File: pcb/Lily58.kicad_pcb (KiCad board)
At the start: 2 copper layers, 142.5 x 106.3 mm, 112 parts, among them P4 OLED, SW1 SW_PUSH, SW10 SW_PUSH, SW11 SW_PUSH, SW12 SW_PUSH, SW13 SW_PUSH, SW14 SW_PUSH, SW15 SW_PUSH, SW16 SW_PUSH, SW17 SW_PUSH, SW18 SW_PUSH, SW19 SW_PUSH, SW2 SW_PUSH, SW20 SW_PUSH, SW21 SW_PUSH, SW22 SW_PUSH, SW23 SW_PUSH, SW24 SW_PUSH, SW25 Rotary_Encoder_Switch, SW26 SW_PUSH, SW27 SW_PUSH, SW28 SW_PUSH, SW29 SW_PUSH, SW3 SW_PUSH, SW4 SW_PUSH, SW5 SW_PUSH, SW6 SW_PUSH, SW7 SW_PUSH, SW8 SW_PUSH, SW9 SW_PUSH, U1 NiceNano

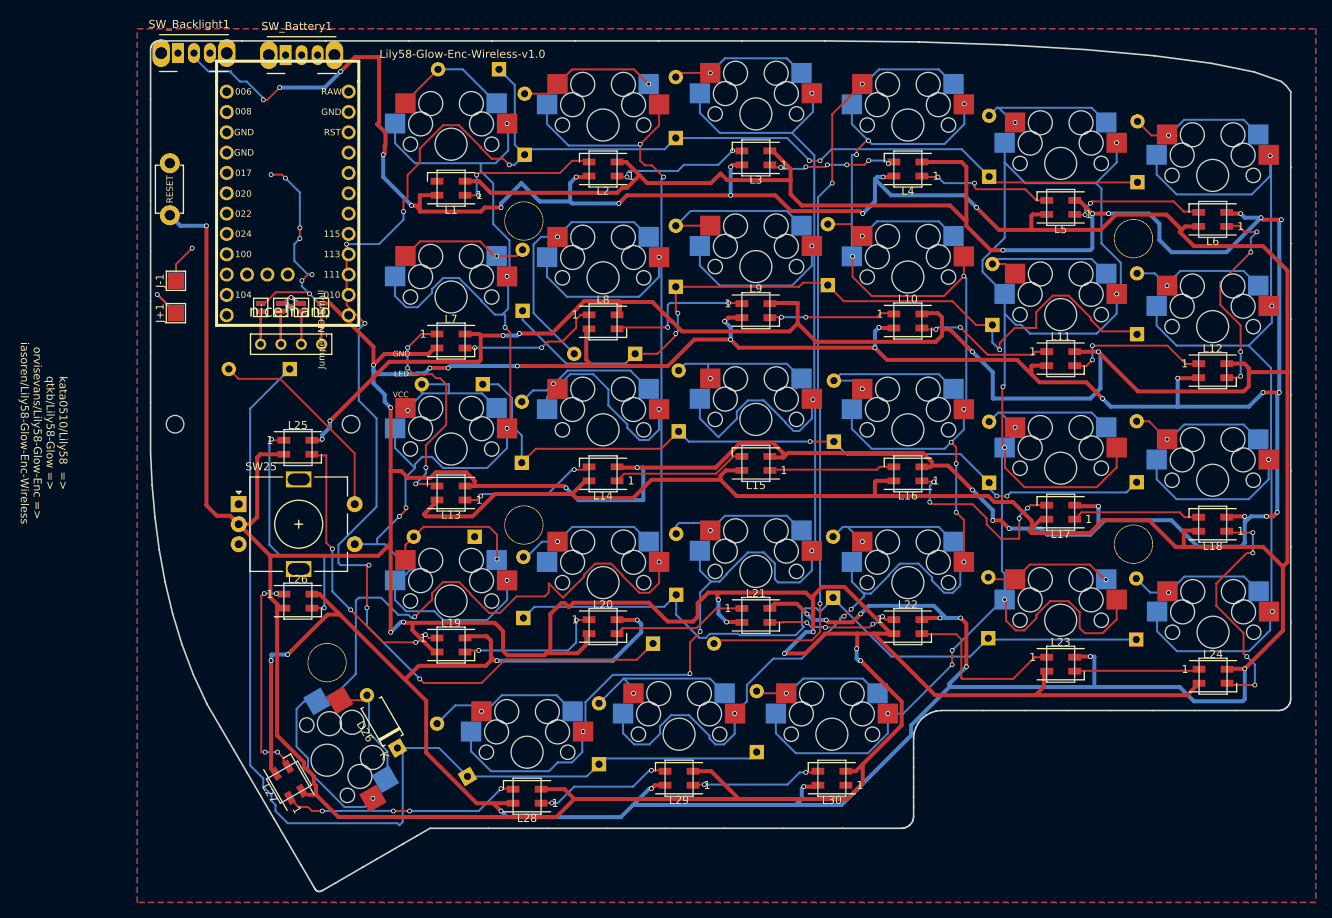
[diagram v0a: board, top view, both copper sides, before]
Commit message: File Cleanup
Worked a bit more on LEDs, started initial firmware settings. Ordered some nice!nanos and soon to have prototype boards in to work with
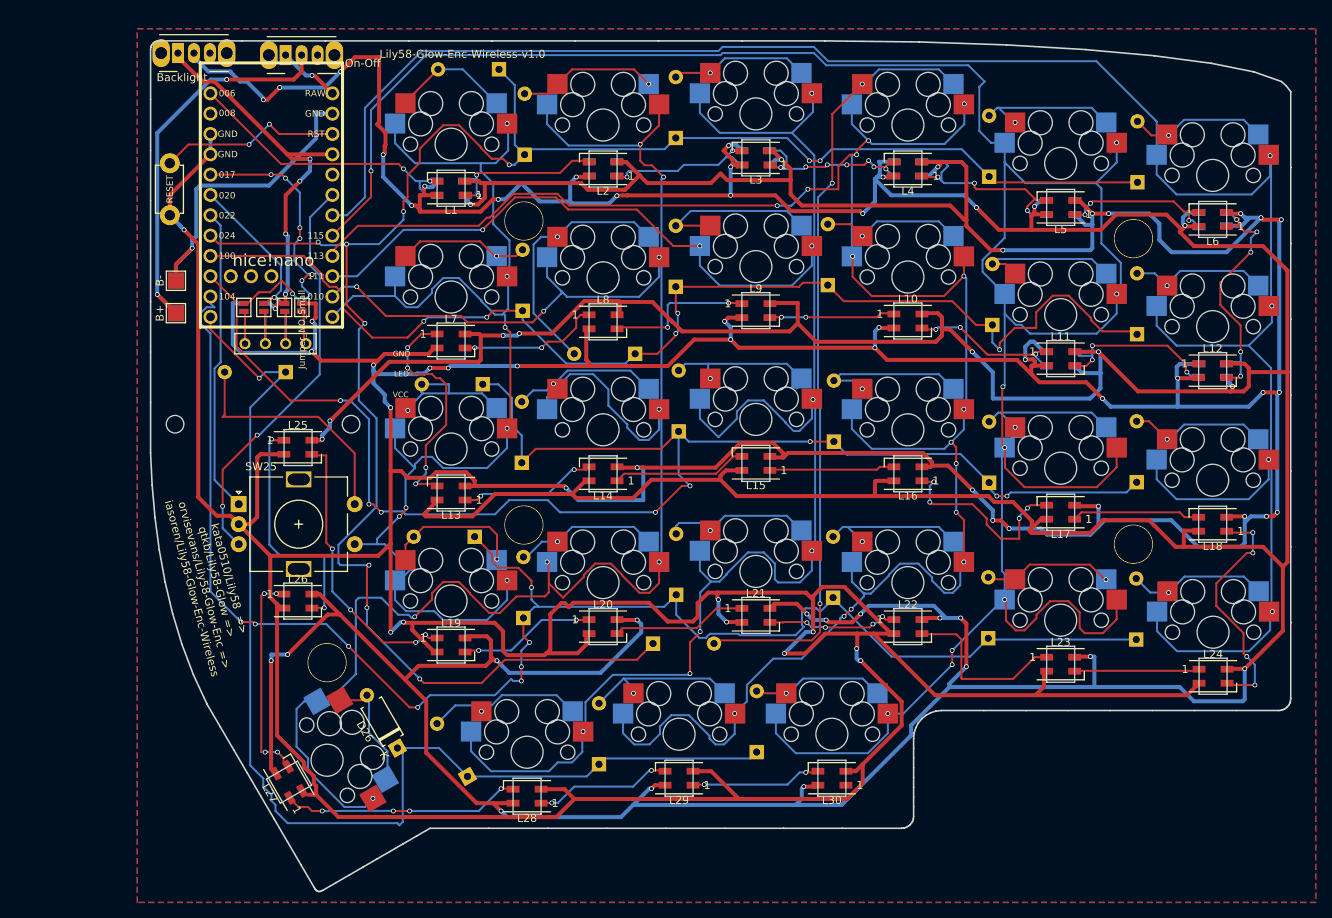
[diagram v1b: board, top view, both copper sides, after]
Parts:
- added ?: , , B.Cu at (198.5, 57.0)
- added ?: , , B.Cu at (118.7, 56.4)
- added ?: , , B.Cu at (179.3, 52.2)
- added ?: , , B.Cu at (156.8, 52.6)
- added ?: , , B.Cu at (141.2, 52.2)
- added ?: , , B.Cu at (160.3, 50.8)
- added ?: , , B.Cu at (194.9, 77.7)
- added ?: , , B.Cu at (213.9, 79.1)
- added ?: , , B.Cu at (214.0, 60.3)
- added ?: , , B.Cu at (122.2, 54.6)
- added ?: , , B.Cu at (214.0, 58.5)
- added ?: , , B.Cu at (194.9, 75.9)
- added ?: , , B.Cu at (175.8, 54.0)
- added ?: , , B.Cu at (122.3, 56.4)
- added ?: , , B.Cu at (198.5, 75.9)
- added ?: , , B.Cu at (137.8, 52.2)
- added ?: , , B.Cu at (198.5, 58.8)
- added ?: , , B.Cu at (217.4, 58.5)
- added ?: , , B.Cu at (217.4, 79.1)
- added ?: , , B.Cu at (217.4, 60.2)
- added ?: , , B.Cu at (217.4, 77.5)
- added ?: , , B.Cu at (141.2, 54.0)
- added ?: , , B.Cu at (194.9, 58.8)
- added ?: , , B.Cu at (198.5, 77.7)
- added ?: , , B.Cu at (175.9, 52.2)
- added ?: , , B.Cu at (194.9, 57.0)
- added ?: , , B.Cu at (118.7, 54.6)
- added ?: , , B.Cu at (156.8, 50.8)
- added ?: , , B.Cu at (214.0, 77.5)
- added ?: , , B.Cu at (137.8, 54.0)
- added ?: , , B.Cu at (160.4, 52.6)
- added ?: , , B.Cu at (179.3, 54.0)
- moved JP5 2.45 mm to (101.9, 70.4)
- moved JP1 2.45 mm to (101.9, 70.4)
- moved JP3 2.11 mm to (97.1, 70.4)
- moved JP4 2.11 mm to (94.6, 70.4)
- moved JP7 2.11 mm to (97.1, 70.4)
- moved JP8 2.11 mm to (94.6, 70.4)
- moved JP2 2.11 mm to (99.7, 70.4)
- moved JP6 2.11 mm to (99.7, 70.4)
- moved U1 2.04 mm to (98.0, 57.6)
- moved P4 1.96 mm to (94.7, 74.9)
- moved D25 0.63 mm to (99.8, 78.5)
- renumbered J+1 to B+, J-1 to B-, SW_Backlight1 to Backlight, SW_Battery1 to On-Off
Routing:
- net col0: track 138.2 -> 264.5 mm
- net col1: track 208.2 -> 317.3 mm, vias 8 -> 9
- net row3: track 89.3 -> 196.7 mm, vias 0 -> 8
- net row2: track 95.5 -> 187.4 mm, vias 3 -> 8
- net col2: track 182.9 -> 256.4 mm, vias 13 -> 15
- net GND: track 915.5 -> 974.0 mm, vias 37 -> 43
- net col3: track 197.2 -> 249.7 mm, vias 7 -> 9
- net enc2: track 0.00 -> 51.3 mm, vias 0 -> 2
- net VCC: track 3.30 -> 50.3 mm, vias 1 -> 5
- net row1: track 98.6 -> 144.7 mm, vias 3 -> 5
- net Net-(J+1-Pad1): track 6.61 -> 50.1 mm, vias 1 -> 2
- net enc1: track 0.00 -> 38.2 mm
- net LEDunder: track 0.00 -> 35.8 mm, vias 0 -> 2
- net col4: track 211.6 -> 246.9 mm, vias 7 -> 10
- net Batt-: track 9.83 -> 41.2 mm
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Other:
- board text added: "1"
- board text added: "B+"
- board text added: "B-"
- board text added: "Backlight"
- board text added: "On-Off"
- board text removed: "J+1"
- board text removed: "J-1"

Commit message: Backlight LEDs
Finished the routing for backlight LEDs, adjusted nice!nano placement and power placement. Moved some text around to empty board spots, made sure that silkscreen was duplicated to both sides. Uploaded gerber files along with drill plots for JLCPCB. I will run a GB at some point in the next month if all goes well.
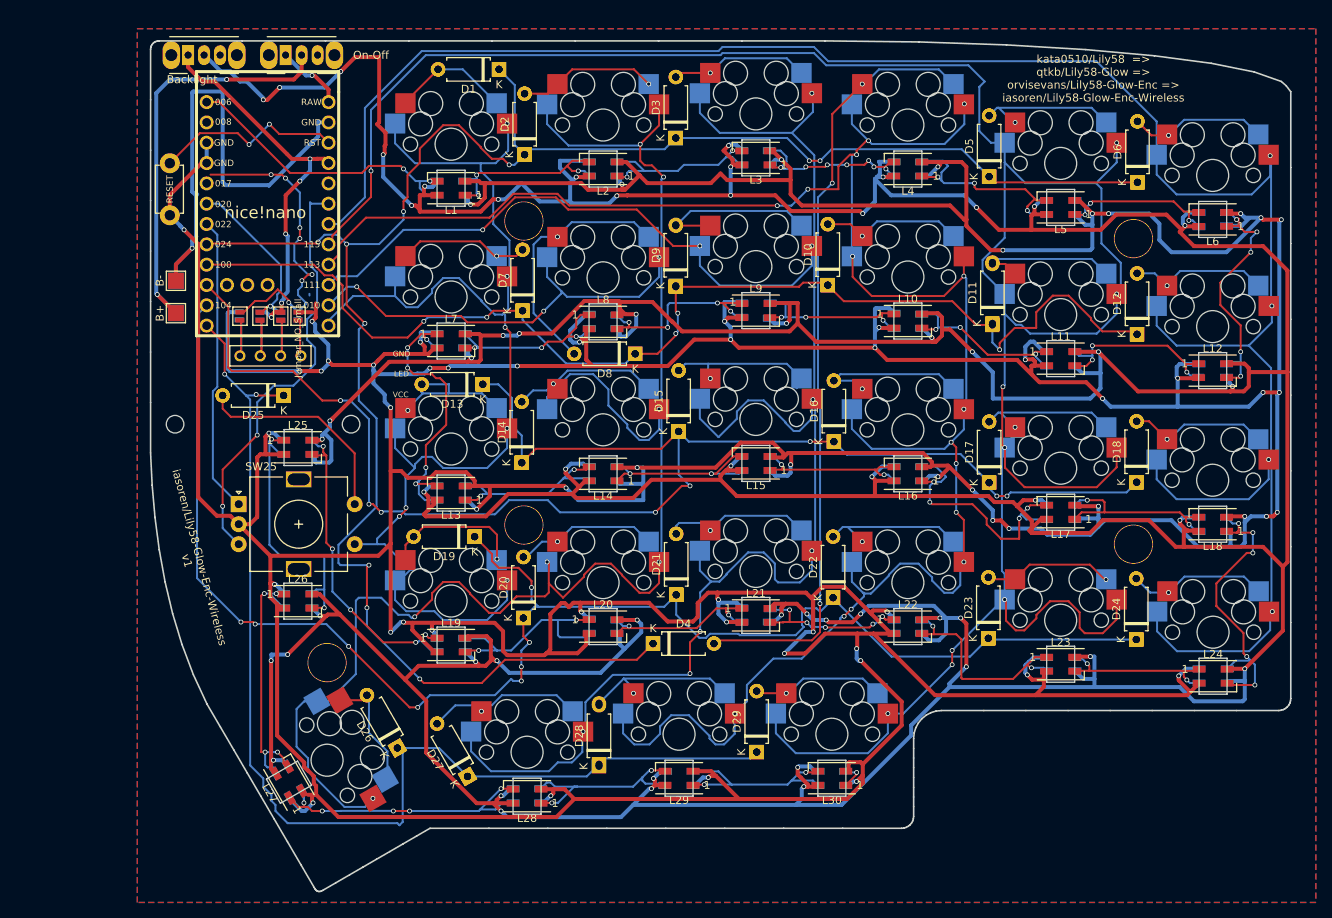
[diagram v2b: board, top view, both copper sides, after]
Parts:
- added ?: , , B.Cu at (198.5, 115.8)
- added ?: , , B.Cu at (118.7, 111.8)
- added ?: , , B.Cu at (122.3, 113.4)
- added ?: , , B.Cu at (160.4, 108.1)
- added ?: , , B.Cu at (160.4, 89.0)
- added ?: , , B.Cu at (100.1, 127.8)
- added ?: , , B.Cu at (194.9, 115.8)
- added ?: , , B.Cu at (179.3, 92.1)
- added ?: , , B.Cu at (150.7, 128.4)
- added ?: , , B.Cu at (118.7, 94.5)
- added ?: , , B.Cu at (156.8, 71.6)
- added ?: , , B.Cu at (141.2, 109.5)
- added ?: , , B.Cu at (179.3, 111.1)
- added ?: , , B.Cu at (169.8, 130.2)
- added ?: , , B.Cu at (175.9, 73.0)
- added ?: , , B.Cu at (118.7, 75.4)
- added ?: , , B.Cu at (137.8, 90.3)
- added ?: , , B.Cu at (160.4, 90.8)
- added ?: , , B.Cu at (179.3, 71.2)
- added ?: , , B.Cu at (118.7, 73.7)
- added ?: , , B.Cu at (122.3, 92.7)
- added ?: , , B.Cu at (166.4, 130.2)
- added ?: , , B.Cu at (131.7, 132.3)
- added ?: , , B.Cu at (137.8, 111.1)
- added ?: , , B.Cu at (194.9, 95.1)
- added ?: , , B.Cu at (214.0, 115.6)
- added ?: , , B.Cu at (217.4, 96.6)
- added ?: , , B.Cu at (147.2, 130.2)
- added ?: , , B.Cu at (100.3, 131.7)
- added ?: , , B.Cu at (179.3, 109.5)
- added ?: , , B.Cu at (198.5, 96.9)
- added ?: , , B.Cu at (141.2, 71.4)
- added ?: , , B.Cu at (122.3, 73.7)
- added ?: , , B.Cu at (141.2, 90.3)
- added ?: , , B.Cu at (156.8, 89.0)
- added ?: , , B.Cu at (137.8, 73.0)
- added ?: , , B.Cu at (99.6, 106.2)
- added ?: , , B.Cu at (98.6, 128.7)
- added ?: , , B.Cu at (217.6, 117.3)
- added ?: , , B.Cu at (160.3, 109.7)
- added ?: , , B.Cu at (214.0, 98.4)
- added ?: , , B.Cu at (103.1, 88.8)
- added ?: , , B.Cu at (99.6, 108.0)
- added ?: , , B.Cu at (122.3, 94.5)
- added ?: , , B.Cu at (156.8, 69.8)
- added ?: , , B.Cu at (103.1, 106.2)
- added ?: , , B.Cu at (141.2, 92.1)
- added ?: , , B.Cu at (169.8, 128.4)
- added ?: , , B.Cu at (175.9, 92.1)
- added ?: , , B.Cu at (175.9, 109.5)
- added ?: , , B.Cu at (160.3, 71.8)
- added ?: , , B.Cu at (160.4, 69.8)
- added ?: , , B.Cu at (103.1, 87.0)
- added ?: , , B.Cu at (128.3, 130.6)
- added ?: , , B.Cu at (131.7, 130.6)
- added ?: , , B.Cu at (141.2, 111.1)
- added ?: , , B.Cu at (141.2, 73.0)
- added ?: , , B.Cu at (217.6, 115.6)
- added ?: , , B.Cu at (122.2, 111.8)
- added ?: , , B.Cu at (214.0, 117.3)
- added ?: , , B.Cu at (103.1, 108.0)
- added ?: , , B.Cu at (147.3, 128.4)
- added ?: , , B.Cu at (99.6, 88.8)
- added ?: , , B.Cu at (194.9, 96.9)
- added ?: , , B.Cu at (175.9, 71.1)
- added ?: , , B.Cu at (179.3, 73.0)
- added ?: , , B.Cu at (128.3, 132.3)
- added ?: , , B.Cu at (166.4, 128.4)
- added ?: , , B.Cu at (214.0, 96.6)
- added ?: , , B.Cu at (156.8, 108.0)
- added ?: , , B.Cu at (99.6, 87.0)
- added ?: , , B.Cu at (179.3, 90.3)
- added ?: , , B.Cu at (137.8, 71.2)
- added ?: , , B.Cu at (198.5, 114.2)
- added ?: , , B.Cu at (217.4, 98.4)
- added ?: , , B.Cu at (137.8, 92.1)
- added ?: , , B.Cu at (175.9, 111.1)
- added ?: , , B.Cu at (118.7, 92.7)
- added ?: , , B.Cu at (118.7, 113.4)
- added ?: , , B.Cu at (198.5, 95.1)
- added ?: , , B.Cu at (150.7, 130.2)
- added ?: , , B.Cu at (194.9, 114.2)
- added ?: , , B.Cu at (175.9, 90.3)
- added ?: , , B.Cu at (137.8, 109.3)
- added ?: , , B.Cu at (122.2, 75.4)
- added ?: , , B.Cu at (156.8, 109.7)
- added ?: , , B.Cu at (101.9, 130.8)
- added ?: , , B.Cu at (156.8, 90.8)
- added D1: D, Diode_THT:D_A-405_P7.62mm_Horizontal, F.Cu at (126.5, 40.6)
- added D10: D, Diode_THT:D_A-405_P7.62mm_Horizontal, F.Cu at (167.6, 67.6)
- added D11: D, Diode_THT:D_A-405_P7.62mm_Horizontal, F.Cu at (188.2, 72.4)
- added D12: D, Diode_THT:D_A-405_P7.62mm_Horizontal, F.Cu at (206.2, 73.8)
- added D13: D, Diode_THT:D_A-405_P7.62mm_Horizontal, F.Cu at (124.5, 80.0)
- added D14: D, Diode_THT:D_A-405_P7.62mm_Horizontal, F.Cu at (129.3, 89.8)
- added D15: D, Diode_THT:D_A-405_P7.62mm_Horizontal, F.Cu at (148.9, 85.9)
- added D16: D, Diode_THT:D_A-405_P7.62mm_Horizontal, F.Cu at (168.4, 87.2)
- added D17: D, Diode_THT:D_A-405_P7.62mm_Horizontal, F.Cu at (187.8, 92.3)
- added D18: D, Diode_THT:D_A-405_P7.62mm_Horizontal, F.Cu at (206.2, 92.3)
- added D19: D, Diode_THT:D_A-405_P7.62mm_Horizontal, F.Cu at (123.4, 99.1)
- added D2: D, Diode_THT:D_A-405_P7.62mm_Horizontal, F.Cu at (129.7, 51.3)
- added D20: D, Diode_THT:D_A-405_P7.62mm_Horizontal, F.Cu at (129.5, 109.2)
- added D21: D, Diode_THT:D_A-405_P7.62mm_Horizontal, F.Cu at (148.6, 106.3)
- added D22: D, Diode_THT:D_A-405_P7.62mm_Horizontal, F.Cu at (168.2, 106.7)
- added D23: D, Diode_THT:D_A-405_P7.62mm_Horizontal, F.Cu at (187.7, 111.8)
- added D24: D, Diode_THT:D_A-405_P7.62mm_Horizontal, F.Cu at (206.1, 111.9)
- added D25: D, Diode_THT:D_A-405_P7.62mm_Horizontal, F.Cu at (99.6, 81.4)
- added D26: D, Diode_THT:D_A-405_P7.62mm_Horizontal, B.Cu at (113.8, 125.5)
- added D27: D, Diode_THT:D_A-405_P7.62mm_Horizontal, F.Cu at (122.6, 129.0)
- added D28: D, Diode_THT:D_A-405_P7.62mm_Horizontal, F.Cu at (139.0, 127.8)
- added D29: D, Diode_THT:D_A-405_P7.62mm_Horizontal, F.Cu at (158.7, 126.0)
- added D3: D, Diode_THT:D_A-405_P7.62mm_Horizontal, F.Cu at (148.6, 49.2)
- added D4: D, Diode_THT:D_A-405_P7.62mm_Horizontal, F.Cu at (145.7, 112.4)
- added D5: D, Diode_THT:D_A-405_P7.62mm_Horizontal, F.Cu at (187.8, 54.1)
- added D6: D, Diode_THT:D_A-405_P7.62mm_Horizontal, F.Cu at (206.3, 54.8)
- added D7: D, Diode_THT:D_A-405_P7.62mm_Horizontal, F.Cu at (129.4, 70.8)
- added D8: D, Diode_THT:D_A-405_P7.62mm_Horizontal, F.Cu at (143.5, 76.2)
- added D9: D, Diode_THT:D_A-405_P7.62mm_Horizontal, F.Cu at (148.6, 67.7)
- moved D25 2.93 mm to (99.6, 81.4)
- moved P4 1.65 mm to (94.1, 76.5)
- moved Backlight 1.29 mm to (87.6, 38.9)
- moved JP8 1.20 mm to (94.0, 71.5)
- moved U1 1.19 mm to (97.6, 58.7)
- moved JP2 1.19 mm to (99.2, 71.5)
- moved JP6 1.19 mm to (99.2, 71.5)
- moved JP1 1.19 mm to (101.4, 71.5)
- moved JP3 1.19 mm to (96.6, 71.5)
- moved JP4 1.19 mm to (94.1, 71.5)
- moved JP5 1.19 mm to (101.4, 71.5)
- moved JP7 1.19 mm to (96.6, 71.5)
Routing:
- net GND: track 974.0 -> 1065.3 mm, vias 43 -> 62
- net Net-(L1-Pad4): track 841.0 -> 926.8 mm, vias 39 -> 56
- net Batt-: track 41.2 -> 62.8 mm
- net Net-(L19-Pad3): track 16.6 -> 27.1 mm
- net Net-(L29-Pad1): track 15.8 -> 24.5 mm
- net Net-(L28-Pad1): track 16.7 -> 25.0 mm
- net Net-(L16-Pad1): track 24.1 -> 31.9 mm
- net Net-(L17-Pad1): track 15.6 -> 23.2 mm, vias 0 -> 2
- net Net-(L27-Pad1): track 29.3 -> 36.8 mm, vias 4 -> 5
- net Net-(L13-Pad3): track 28.8 -> 35.4 mm, vias 4 -> 5
- net Net-(L13-Pad1): track 16.7 -> 23.0 mm
- net Net-(L18-Pad1): track 29.7 -> 35.9 mm, vias 4 -> 5
- net Net-(L21-Pad3): track 16.1 -> 22.3 mm, vias 4 -> 5
- net Net-(L8-Pad3): track 18.1 -> 24.1 mm, vias 2 -> 4
- net Net-(L10-Pad1): track 15.3 -> 21.2 mm, vias 2 -> 3
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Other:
- rule pad_to_mask_clearance: 0.2 -> 0
- board text added: "L1"
- board text added: "L10"
- board text added: "L11"
- board text added: "L12"
- board text added: "L13"
- board text added: "L14"
- board text added: "L15"
- board text added: "L16"
- board text added: "L17"
- board text added: "L18"
- board text added: "L19"
- board text added: "L2"
- board text added: "L20"
- board text added: "L21"
- board text added: "L22"
- board text added: "L23"
- board text added: "L24"
- board text added: "L25"
- board text added: "L26"
- board text added: "L27"
- board text added: "L28"
- board text added: "L29"
- board text added: "L3"
- board text added: "L30"
- board text added: "L4"
- board text added: "L5"
- board text added: "L6"
- board text added: "L7"
- board text added: "L8"
- board text added: "L9"
- board text added: "iasoren/Lily58-Glow-Enc-Wireless v1"
- board text removed: "Lily58-Glow-Enc-Wireless-v1.0"
